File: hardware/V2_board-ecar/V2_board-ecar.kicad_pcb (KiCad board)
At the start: 2 copper layers, 160 x 100 mm, 99 parts, among them IC1 ATMEGA8A-P, J1 2x BATT IN, J10 24V, J11 18V, J12 5V, J13 Analog-in-2 0-5V, J14 IGBT, J15 Analog-in-3 - 30to5 (batt), J17 2x Switch (to 5V), J18 Relay contacts, J19 2x 5V, J2 ST 2x GND, J20 ADC Battery, J21 ADC reserve, J22 ADC Gas-pedal, J23 2x 24V filtered, J24 GND-supp, Diode, Mosfet (fan), J3 2x 24V filtered, J4 ST 2x GND, J5 PWM-Signal, J6 LED ~3,2V 20mA, J7 Gas Pedal, J8 Gate, J9 BATT, K1 LEG-5, P1 ISP, Q1 BC547, Q2 IRFZ24N, Q3 BC547, U1 LM7818CT, U2 LM2576T-5, U3 TC429

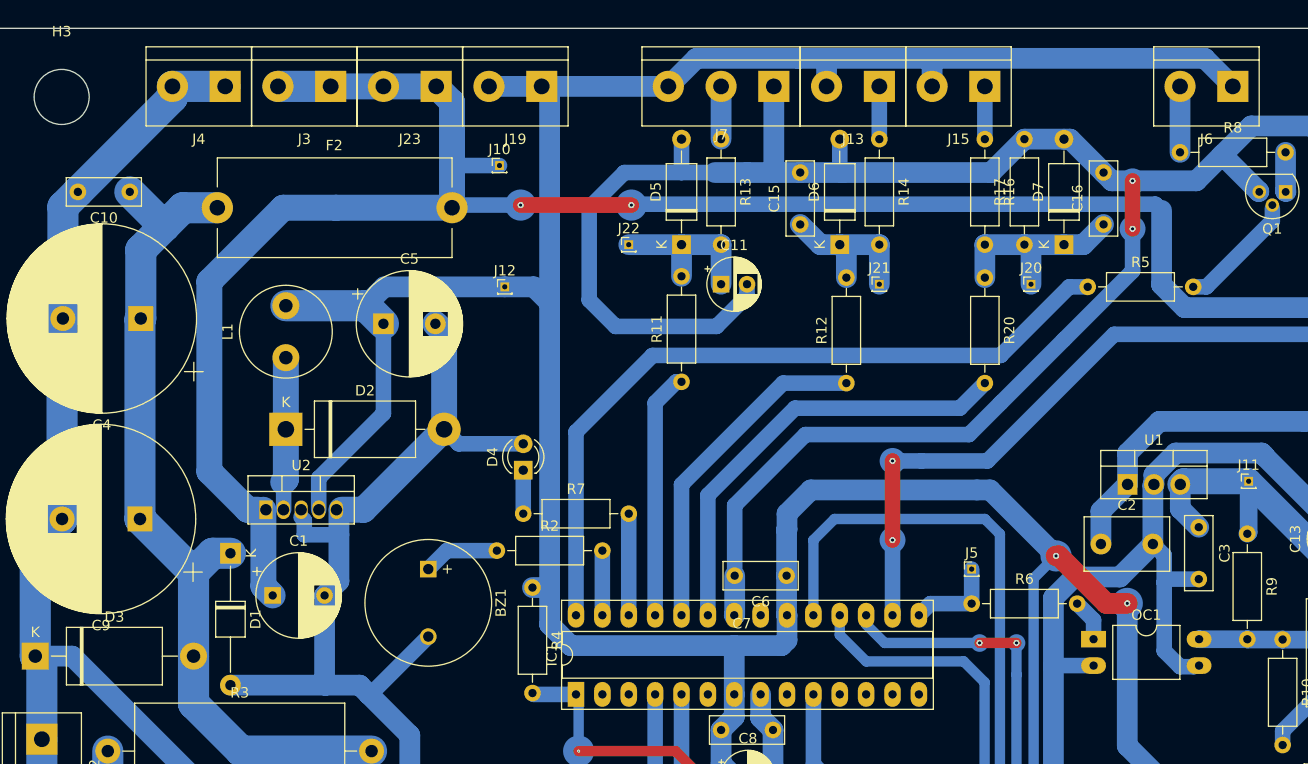
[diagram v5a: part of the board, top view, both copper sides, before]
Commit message: pcb: Fix footprints, add pcb2gcode conf from ihc-control_pcb project
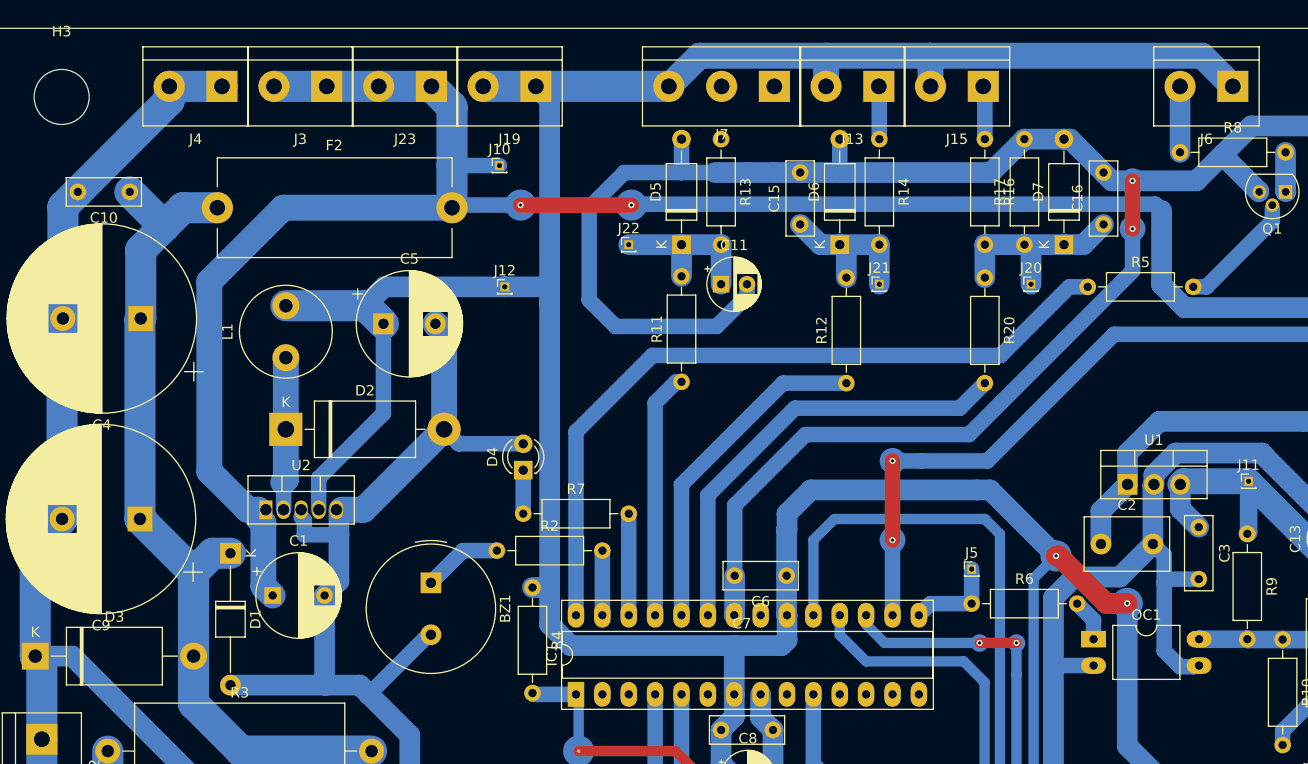
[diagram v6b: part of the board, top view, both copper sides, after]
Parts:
- BZ1: footprint Buzzer_Beeper:MagneticBuzzer_ProSignal_ABT-410-RC -> Buzzer_Beeper:Buzzer_TDK_PS1240P02BT_D12.2mm_H6.5mm
- moved BZ1 1.35 mm to (43.2, 53.4)
- moved J19 0.56 mm to (53.3, 5.59)
- moved J23 0.46 mm to (43.2, 5.59)
- moved J3 0.38 mm to (33.1, 5.59)
- moved J4 0.30 mm to (23.1, 5.59)
- moved J15 0.15 mm to (96.4, 5.59)
- moved J13 0.05 mm to (86.3, 5.59)
- moved J7 0.05 mm to (76.3, 5.59)
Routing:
- net GND: track 888.5 -> 880.5 mm
- net Net-(J7-Pin_2): track 5.08 -> 0.00 mm
- net +5V: track 352.2 -> 353.0 mm

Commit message: pcb: Fix missing tracks, Annotate schematic and layout
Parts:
- D3: value TVS 26V (starts 31V) -> TVS 28V (starts 31V)
- F1: value 500mA -> slow, max 4A
- F3: value 500mA -> (H7 24V 70W) -> 3A
- J14: value IGBT -> IGBT [GND, Gate]
- J18: value Relay contacts -> Relay contacts [NO, COM, NC]
- J24: value GND-supp, Diode, Mosfet (fan) -> Fan [GND-supp, Diode, Mosfet]
- J6: value LED ~3,2V 20mA -> LED 3,2V 20mA [-, +]
- R16: value 150k -> 100k
- R17: value 30k -> 22k
- R9: value 12k -> 12k (15k used)
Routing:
- net GND: track 880.5 -> 888.8 mm
- net Net-(J7-Pin_2): track 0.00 -> 5.10 mm
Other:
- board text added: "(5mm LED 3,2V 20mA) (Pin-28/PC5) - +"
- board text added: "20-35V with peaks"
- board text added: "24V 24V"
- board text added: "2x Switch to 5V (Pin-4 / PD2), (Pin-5 / PD3)"
- board text added: "5V 5V"
- board text added: "Analog_0-30V (Pin-23/PC0) 5V(out), 24V(in)"
- board text added: "Analog_0-5V (Pin-24/PC1) 5V, A(in)"
- board text added: "Analog_gas (Pin-25/PC2) 5V, Pedal, GND"
- board text added: "FUSE 24V Filtered"
- board text added: "FUSE Batt Input (Filter)"
- board text added: "FUSE Mosfet"
- board text added: "FUSE Relay Output"
- board text added: "Fan GND(in/out), Fan+(in), Fan-(out) (Pin-16/PB2)"
- board text added: "GND GND"
- board text added: "GND, Gate IGBT (Pin-16/PB2)"
- board text added: "NO, COM, NC Relay (Pin-10/PB7)"
- board text added: "PCB Supply: BATT, BATT"
- board text added: "PCB Supply: GND GND"
